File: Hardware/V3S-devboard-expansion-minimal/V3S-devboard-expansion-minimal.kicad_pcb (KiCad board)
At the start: 2 copper layers, 22 x 4 mm, 2 parts, among them CN1 AS0BC21-S30BE-7H, CN2 AS0BC21-S30BE-7H

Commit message: expansion board work
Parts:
- added C1: 100n, Capacitor_SMD:C_0603_1608Metric, F.Cu at (141.1, 61.7)
- added C10: 10u, Capacitor_SMD:C_0603_1608Metric, F.Cu at (145.1, 64.2)
- added C2: 100n, Capacitor_SMD:C_0603_1608Metric, F.Cu at (141.1, 64.2)
- added C3: 10u, Capacitor_SMD:C_0603_1608Metric, F.Cu at (141.1, 66.8)
- added C4: 1u, Capacitor_SMD:C_0603_1608Metric, F.Cu at (141.1, 69.3)
- added C5: 10u, Capacitor_SMD:C_0603_1608Metric, F.Cu at (141.1, 71.8)
- added C6: 1u, Capacitor_SMD:C_0603_1608Metric, F.Cu at (141.1, 74.3)
- added C7: 10u, Capacitor_SMD:C_0603_1608Metric, F.Cu at (141.1, 76.8)
- added C8: 10u, Capacitor_SMD:C_0603_1608Metric, F.Cu at (141.1, 79.3)
- added C9: 10u, Capacitor_SMD:C_0603_1608Metric, F.Cu at (145.1, 61.7)
- added FPC1: AFC07-S50ECA-00, v3s-devboard-expansion-minimal:FPC-SMD_AFC07-S50ECA-00, F.Cu at (95.5, 42.9)
- added J1: Conn_01x05_Pin, Connector_PinHeader_2.54mm:PinHeader_1x05_P2.54mm_Vertical, F.Cu at (42.3, 60.3)
- added J10: USB_C_Receptacle_USB2.0, Connector_USB:USB_C_Receptacle_HCTL_HC-TYPE-C-16P-01A, F.Cu at (73.6, 117.2)
- added J11: Conn_01x02_Pin, Connector_PinHeader_2.54mm:PinHeader_1x02_P2.54mm_Vertical, F.Cu at (45.6, 47.2)
- added J12: Conn_01x02_Pin, Connector_PinHeader_2.54mm:PinHeader_1x02_P2.54mm_Vertical, F.Cu at (50.3, 47.2)
- added J13: Conn_01x03_Pin, Connector_PinSocket_2.54mm:PinSocket_1x03_P2.54mm_Vertical, F.Cu at (31.2, 58.8)
- added J2: Conn_01x05_Pin, Connector_PinHeader_2.54mm:PinHeader_1x05_P2.54mm_Vertical, F.Cu at (47.0, 60.3)
- added J3: Conn_01x05_Pin, Connector_PinHeader_2.54mm:PinHeader_1x05_P2.54mm_Vertical, F.Cu at (51.6, 60.3)
- added J4: Conn_01x02_Pin, Connector_PinHeader_2.54mm:PinHeader_1x02_P2.54mm_Vertical, F.Cu at (36.3, 47.2)
- added J5: Conn_02x05_Odd_Even, Connector_PinHeader_2.54mm:PinHeader_2x05_P2.54mm_Vertical, F.Cu at (56.4, 40.5)
- added J6: Conn_01x02_Pin, Connector_PinHeader_2.54mm:PinHeader_1x02_P2.54mm_Vertical, F.Cu at (41.0, 47.2)
- added J7: Conn_02x12_Odd_Even, Connector_PinSocket_2.54mm:PinSocket_2x12_P2.54mm_Vertical, F.Cu at (36.0, 90.2)
- added J8: RJ45_Hanrun_HR911105A_Horizontal, Connector_RJ:RJ45_Hanrun_HR911105A_Horizontal, F.Cu at (108.8, 103.4)
- added J9: Conn_02x03_Odd_Even, Connector_PinSocket_2.54mm:PinSocket_2x03_P2.54mm_Vertical, F.Cu at (31.7, 41.6)
- added L1: 2.2u, Inductor_SMD:L_1008_2520Metric, F.Cu at (153.6, 62.4)
- added R1: 100, Resistor_SMD:R_0603_1608Metric, F.Cu at (145.1, 66.8)
- added R10: 51, Resistor_SMD:R_0603_1608Metric, F.Cu at (149.1, 66.8)
- added R11: 51, Resistor_SMD:R_0603_1608Metric, F.Cu at (149.1, 69.3)
- added R12: 5.1K, Resistor_SMD:R_0603_1608Metric, F.Cu at (149.1, 71.8)
- added R13: 4.7K, Resistor_SMD:R_0603_1608Metric, F.Cu at (149.1, 74.3)
- added R14: 5.1K, Resistor_SMD:R_0603_1608Metric, F.Cu at (149.1, 76.8)
- added R2: 100, Resistor_SMD:R_0603_1608Metric, F.Cu at (145.1, 69.3)
- added R3: 100, Resistor_SMD:R_0603_1608Metric, F.Cu at (145.1, 71.8)
- added R4: 100, Resistor_SMD:R_0603_1608Metric, F.Cu at (145.1, 74.3)
- added R5: 680, Resistor_SMD:R_0603_1608Metric, F.Cu at (145.1, 76.8)
- added R6: 10k, Resistor_SMD:R_0402_1005Metric, F.Cu at (152.6, 65.2)
- added R7: 680, Resistor_SMD:R_0603_1608Metric, F.Cu at (145.1, 79.3)
- added R8: 51, Resistor_SMD:R_0603_1608Metric, F.Cu at (149.1, 61.7)
- added R9: 51, Resistor_SMD:R_0603_1608Metric, F.Cu at (149.1, 64.2)
- added U1: CP2102N-Axx-xQFN28, Package_DFN_QFN:QFN-28-1EP_5x5mm_P0.5mm_EP3.1x3.1mm, F.Cu at (57.6, 99.0)
- added U2: XDFC-0522-50P, v3s-devboard-expansion-minimal:FPC-SMD_50P-P0.50_LX_XDFC-0522-50P, F.Cu at (95.5, 50.8)
- added U3: AMS1117-3.3, Package_TO_SOT_SMD:SOT-223-3_TabPin2, F.Cu at (78.4, 97.9)
- added U4: AMS1117-2.85, Package_TO_SOT_SMD:SOT-223-3_TabPin2, F.Cu at (70.1, 97.9)
- moved CN2 37.3 mm to (153.9, 112.7)
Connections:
- CN1 pad 76: unconnected-(CN1-Pad76) -> GND
- CN1 pad 77: unconnected-(CN1-Pad77) -> GND

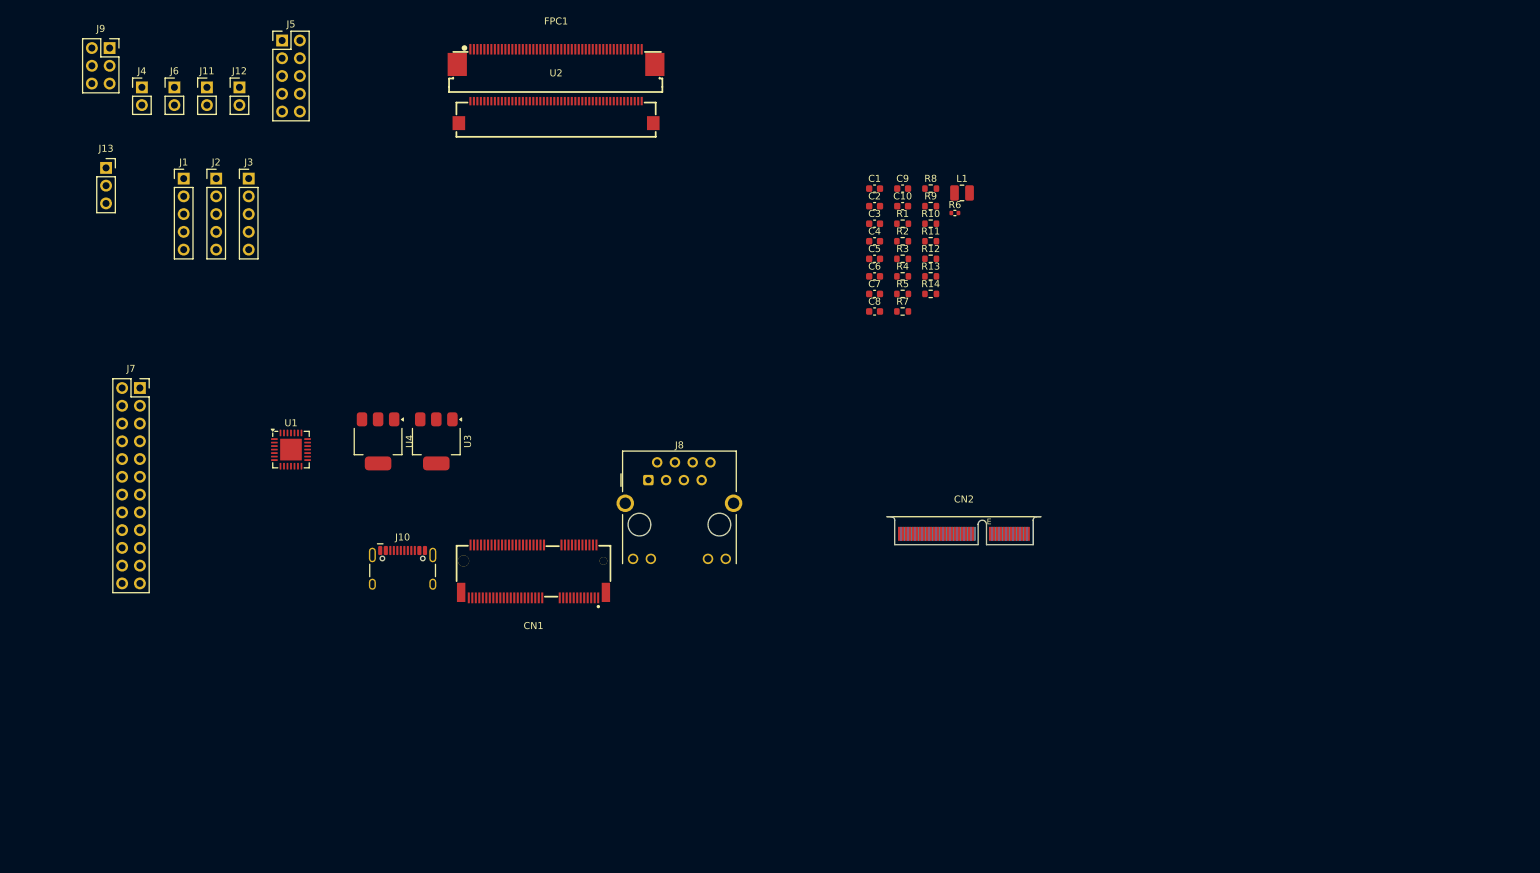
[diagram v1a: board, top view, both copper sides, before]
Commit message: expansion layout and schematic
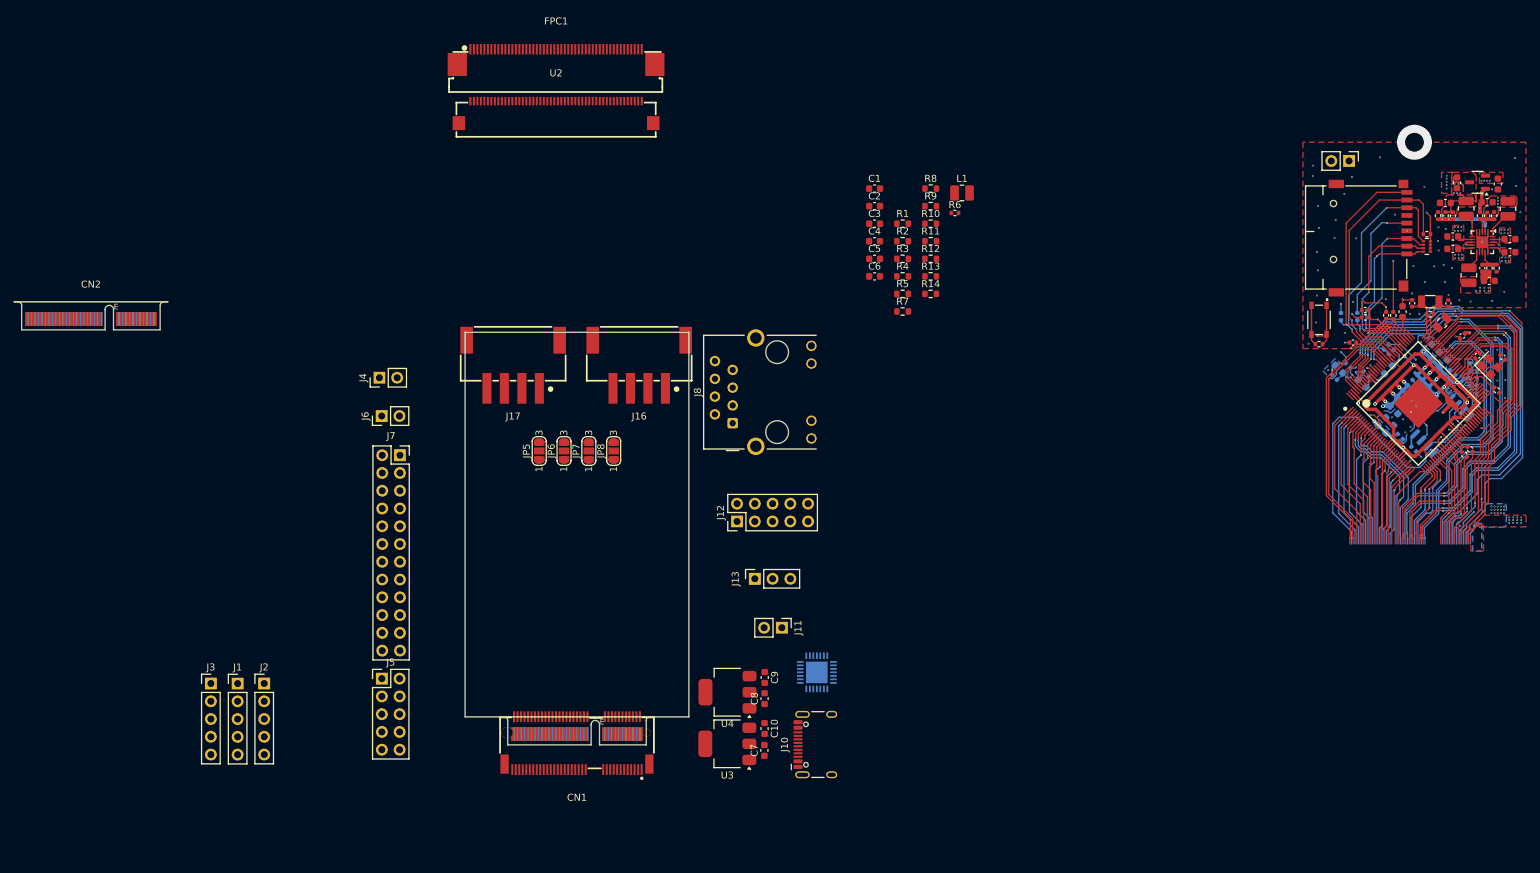
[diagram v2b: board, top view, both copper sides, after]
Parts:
- removed J9: Conn_02x03_Odd_Even, Connector_PinSocket_2.54mm:PinSocket_2x03_P2.54mm_Vertical
- added C101: 1u, Capacitor_SMD:C_0603_1608Metric, F.Cu at (231.9, 70.8)
- added C102: 10u, Capacitor_SMD:C_0603_1608Metric, F.Cu at (231.9, 69.0)
- added C103: 10u, Capacitor_SMD:C_0603_1608Metric, F.Cu at (223.8, 70.3)
- added C104: 10u, Capacitor_SMD:C_0603_1608Metric, F.Cu at (223.8, 68.6)
- added C105: 18p, Capacitor_SMD:C_0402_1005Metric, F.Cu at (228.0, 73.1)
- added C106: 1u, Capacitor_SMD:C_0603_1608Metric, F.Cu at (224.4, 60.9)
- added C107: 1u, Capacitor_SMD:C_0603_1608Metric, F.Cu at (230.2, 61.1)
- added C108: 18p, Capacitor_SMD:C_0402_1005Metric, F.Cu at (223.8, 65.6)
- added C109: 10u, Capacitor_SMD:C_0603_1608Metric, F.Cu at (222.7, 63.8)
- added C110: 18p, Capacitor_SMD:C_0402_1005Metric, F.Cu at (228.7, 65.6)
- added C111: 10u, Capacitor_SMD:C_0603_1608Metric, F.Cu at (228.7, 63.7)
- added C201: 100n, Capacitor_SMD:C_0402_1005Metric, B.Cu at (226.7, 91.1)
- added C202: 100n, Capacitor_SMD:C_0402_1005Metric, B.Cu at (226.7, 89.9)
- added C203: 10u, Capacitor_SMD:C_0603_1608Metric, B.Cu at (221.3, 85.6)
- added C204: 1u, Capacitor_SMD:C_0603_1608Metric, B.Cu at (222.4, 86.7)
- added C205: 100n, Capacitor_SMD:C_0402_1005Metric, B.Cu at (223.8, 88.7)
- added C206: 1u, Capacitor_SMD:C_0603_1608Metric, B.Cu at (220.2, 84.5)
- added C207: 100n, Capacitor_SMD:C_0402_1005Metric, B.Cu at (223.1, 88.0)
- added C208: 10u, Capacitor_SMD:C_0603_1608Metric, B.Cu at (220.7, 91.9)
- added C209: 1u, Capacitor_SMD:C_0603_1608Metric, B.Cu at (219.6, 90.8)
- added C210: 100n, Capacitor_SMD:C_0402_1005Metric, B.Cu at (219.1, 89.5)
- added C211: 100n, Capacitor_SMD:C_0402_1005Metric, B.Cu at (218.4, 88.8)
- added C212: 10u, Capacitor_SMD:C_0603_1608Metric, B.Cu at (213.7, 95.0)
- added C213: 1u, Capacitor_SMD:C_0603_1608Metric, B.Cu at (214.8, 96.1)
- added C214: 100n, Capacitor_SMD:C_0402_1005Metric, B.Cu at (215.6, 97.2)
- added C215: 100n, Capacitor_SMD:C_0402_1005Metric, B.Cu at (216.3, 97.9)
- added C216: 10u, Capacitor_SMD:C_0603_1608Metric, B.Cu at (216.5, 92.3)
- added C217: 1u, Capacitor_SMD:C_0603_1608Metric, B.Cu at (215.4, 93.4)
- added C218: 100n, Capacitor_SMD:C_0402_1005Metric, B.Cu at (217.7, 90.2)
- added C219: 100n, Capacitor_SMD:C_0402_1005Metric, B.Cu at (217.0, 91.0)
- added C220: 100n, Capacitor_SMD:C_0402_1005Metric, F.Cu at (209.5, 83.8)
- added C221: 100n, Capacitor_SMD:C_0402_1005Metric, F.Cu at (225.2, 82.8)
- added C222: 100n, Capacitor_SMD:C_0402_1005Metric, F.Cu at (214.2, 79.8)
- added C223: 100n, Capacitor_SMD:C_0402_1005Metric, B.Cu at (226.7, 86.7)
- added C224: 100n, Capacitor_SMD:C_0402_1005Metric, B.Cu at (208.8, 87.0)
- added C225: 1u, Capacitor_SMD:C_0603_1608Metric, B.Cu at (214.6, 87.6)
- added C226: 4.7u, Capacitor_SMD:C_0603_1608Metric, B.Cu at (210.8, 89.6)
- added C227: 10u, Capacitor_SMD:C_0603_1608Metric, B.Cu at (207.5, 87.5)
- added C228: 100n, Capacitor_SMD:C_0402_1005Metric, B.Cu at (206.9, 88.7)
- added C229: 4.7u, Capacitor_SMD:C_0603_1608Metric, F.Cu at (216.6, 79.3)
- added C230: 18p, Capacitor_SMD:C_0402_1005Metric, F.Cu at (218.0, 78.1)
- added C231: 18p, Capacitor_SMD:C_0402_1005Metric, F.Cu at (223.2, 78.2)
- added C232: 18p, Capacitor_SMD:C_0402_1005Metric, F.Cu at (227.3, 85.7)
- added C233: 18p, Capacitor_SMD:C_0402_1005Metric, F.Cu at (230.9, 85.8)
- added C234: 100n, Capacitor_SMD:C_0402_1005Metric, F.Cu at (211.2, 79.1)
- added C235: 100n, Capacitor_SMD:C_0402_1005Metric, B.Cu at (215.0, 85.1)
- added C236: 100n, Capacitor_SMD:C_0402_1005Metric, B.Cu at (218.2, 99.0)
- added Ce101: 10u, Capacitor_SMD:C_0603_1608Metric, F.Cu at (229.0, 74.9)
- added J101: Conn_01x02, Connector_PinHeader_2.54mm:PinHeader_1x02_P2.54mm_Vertical, F.Cu at (208.9, 57.8)
- added J16: Conn_01x04_MountingPin, v3s-devboard-expansion-minimal:CONN-SMD_HCZZ0021-4, F.Cu at (107.4, 86.8)
- added J17: Conn_01x04_MountingPin, v3s-devboard-expansion-minimal:CONN-SMD_HCZZ0021-4, F.Cu at (89.4, 86.8)
- added J201: Micro_SD_Card_Det1, v3s-devboard-module:J_sd_micro_socket, F.Cu at (210.2, 67.8)
- added J301: AS0BC21-S30BE-7H, v3s-devboard-module:m2-padKeyE, F.Cu at (98.5, 141.3)
- added JP5: SolderJumper_3_Open, Jumper:SolderJumper-3_P1.3mm_Open_RoundedPad1.0x1.5mm_NumberLabels, F.Cu at (93.1, 99.2)
- added JP6: SolderJumper_3_Open, Jumper:SolderJumper-3_P1.3mm_Open_RoundedPad1.0x1.5mm_NumberLabels, F.Cu at (96.7, 99.2)
- added JP7: SolderJumper_3_Open, Jumper:SolderJumper-3_P1.3mm_Open_RoundedPad1.0x1.5mm_NumberLabels, F.Cu at (100.2, 99.2)
- added JP8: SolderJumper_3_Open, Jumper:SolderJumper-3_P1.3mm_Open_RoundedPad1.0x1.5mm_NumberLabels, F.Cu at (103.8, 99.2)
- added L101: 2.2u, Inductor_SMD:L_1008_2520Metric, F.Cu at (226.1, 74.1)
- added L102: 2.2u, Inductor_SMD:L_1008_2520Metric, F.Cu at (225.7, 64.6)
- added L103: 2.2u, Inductor_SMD:L_1008_2520Metric, F.Cu at (231.7, 64.6)
- added R101: 200K, Resistor_SMD:R_0402_1005Metric, F.Cu at (229.0, 73.1)
- added R102: 100K, Resistor_SMD:R_0402_1005Metric, F.Cu at (230.1, 73.1)
- added R103: 680K, Resistor_SMD:R_0402_1005Metric, F.Cu at (222.8, 65.6)
- added R104: 150K, Resistor_SMD:R_0402_1005Metric, F.Cu at (221.7, 65.6)
- added R105: 0, Resistor_SMD:R_0402_1005Metric, F.Cu at (215.3, 79.9)
- added R106: 150K, Resistor_SMD:R_0402_1005Metric, F.Cu at (229.7, 65.6)
- added R107: 150K, Resistor_SMD:R_0402_1005Metric, F.Cu at (227.7, 65.6)
- added R201: 2K, Resistor_SMD:R_0402_1005Metric, B.Cu at (226.7, 88.8)
- added R202: 2K, Resistor_SMD:R_0402_1005Metric, B.Cu at (226.7, 87.8)
- added R203: 200K, Resistor_SMD:R_0402_1005Metric, B.Cu at (211.4, 88.2)
- added R204: 10M, Resistor_SMD:R_0402_1005Metric, F.Cu at (220.6, 79.7)
- added R205: 240, Resistor_SMD:R_0402_1005Metric, F.Cu at (230.1, 90.6)
- added R206: 47K, Resistor_SMD:R_0402_1005Metric, F.Cu at (211.3, 80.2)
- added R207: 6K, Resistor_SMD:R_0805_2012Metric, F.Cu at (222.3, 80.9)
- added R208: 100K, Resistor_SMD:R_0402_1005Metric, B.Cu at (214.3, 84.4)
- added R209: 10K, Resistor_SMD:R_0402_1005Metric, B.Cu at (219.0, 93.9)
- added R210: 0, Resistor_SMD:R_0402_1005Metric, F.Cu at (204.7, 84.0)
- added R211: 33, Resistor_SMD:R_0402_1005Metric, B.Cu at (210.1, 80.0)
- added R212: 33, Resistor_SMD:R_0402_1005Metric, F.Cu at (226.2, 99.0)
- added R213: 33, Resistor_SMD:R_0402_1005Metric, F.Cu at (225.4, 99.8)
- added R214: 47K, Resistor_SMD:R_0402_1005Metric, B.Cu at (207.8, 80.0)
- added R215: 10k, Resistor_SMD:R_0402_1005Metric, F.Cu at (220.1, 68.2)
- added RN201: R_Pack04, Resistor_SMD:R_Array_Concave_4x0402, F.Cu at (220.1, 70.0)
- added SW201: SW_MEC_5E, v3s-devboard-module:SW_SKRPACE010, F.Cu at (204.7, 80.5)
- added U101: EA3036C, Package_DFN_QFN:WQFN-20-1EP_3x3mm_P0.4mm_EP1.7x1.7mm, F.Cu at (228.0, 69.4)
- added U102: XC6206PxxxMR, Package_TO_SOT_SMD:SOT-23-3, F.Cu at (227.3, 60.8)
- added U201: V3S, v3s-devboard-module:LQFP-128_L14.0-W14.0-P0.40-LS16.0-BL-EP5.0, F.Cu at (218.8, 92.5)
- added U202: W25Q128JVS, Package_SO:SOIC-8_5.23x5.23mm_P1.27mm, B.Cu at (222.3, 95.6)
- added Y201: Crystal_Small, Crystal:Crystal_SMD_3215-2Pin_3.2x1.5mm, F.Cu at (220.6, 77.9)
- added Y202: Crystal_GND24_Small, Crystal:Crystal_SMD_2520-4Pin_2.5x2.0mm, F.Cu at (229.1, 87.2)
- J12: value Conn_01x02_Pin -> Conn_02x05_Odd_Even; footprint Connector_PinHeader_2.54mm:PinHeader_1x02_P2.54mm_Vertical -> Connector_PinHeader_2.54mm:PinHeader_2x05_P2.54mm_Vertical
- U1: moved to B.Cu
- moved CN2 128.6 mm to (29.0, 81.9)
- moved J11 112.8 mm to (127.8, 124.5), turned to -90 degrees
- moved J13 109.8 mm to (124.0, 117.5), turned to 90 degrees
- moved J12 94.4 mm to (121.4, 109.3), turned to 90 degrees
- moved J5 92.4 mm to (70.6, 131.8)
- moved U1 81.7 mm to (132.8, 130.9), turned to 180 degrees
- moved C10 77.3 mm to (125.4, 138.9), turned to -90 degrees
- moved C9 72.6 mm to (125.4, 131.6), turned to -90 degrees
- moved J1 72.6 mm to (50.0, 132.5)
- moved J2 72.5 mm to (53.8, 132.5)
- moved J3 72.4 mm to (46.2, 132.5)
- moved C7 67.1 mm to (125.3, 142.1), turned to 90 degrees
- moved J10 64.9 mm to (133.9, 141.2), turned to 90 degrees
- moved U4 61.5 mm to (120.1, 133.8), turned to 180 degrees
- moved U3 60.0 mm to (120.0, 141.1), turned to 180 degrees
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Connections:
- J12 pad 2: Net-(J12-Pin_2) -> /UART0.RX
- U1 pad 25: Net-(J12-Pin_1) -> Net-(J12-Pin_3)
- U1 pad 26: Net-(J12-Pin_2) -> Net-(J12-Pin_1)
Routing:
- net (no net): track 0.00 -> 1896.8 mm, vias 0 -> 108
- net GND: track 0.00 -> 120.8 mm, vias 0 -> 98
- net 3V3: track 0.00 -> 91.8 mm, vias 0 -> 31
- net /CSI.MCSI_MCLK: track 0.00 -> 21.5 mm, vias 0 -> 2
- net /LCD_D23: track 0.00 -> 20.4 mm
- net /LCD_D21: track 0.00 -> 19.5 mm
- net /LCD_D19: track 0.00 -> 18.8 mm
- net /LCD_D15: track 0.00 -> 16.8 mm
- net /LCD_D13: track 0.00 -> 15.9 mm
- net /LCD_D11: track 0.00 -> 15.0 mm
- net /LCD_D7: track 0.00 -> 13.8 mm
- net /LCD_D5: track 0.00 -> 13.2 mm
- net /CSI.CSI_SDA: track 0.00 -> 12.6 mm
- net /LCD_D3: track 0.00 -> 12.4 mm
- net 5V: track 0.00 -> 12.0 mm, vias 0 -> 38
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- added copper zone on F.Cu, net (none)
- added copper zone on F.Cu, net 3V3
- added copper zone on F.Cu, net 5V
- added copper zone on B.Cu, net GND
- added copper zone on F.Cu, net GND
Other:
- board size 22 x 4 mm -> 32 x 55 mm

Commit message: expansion board layout
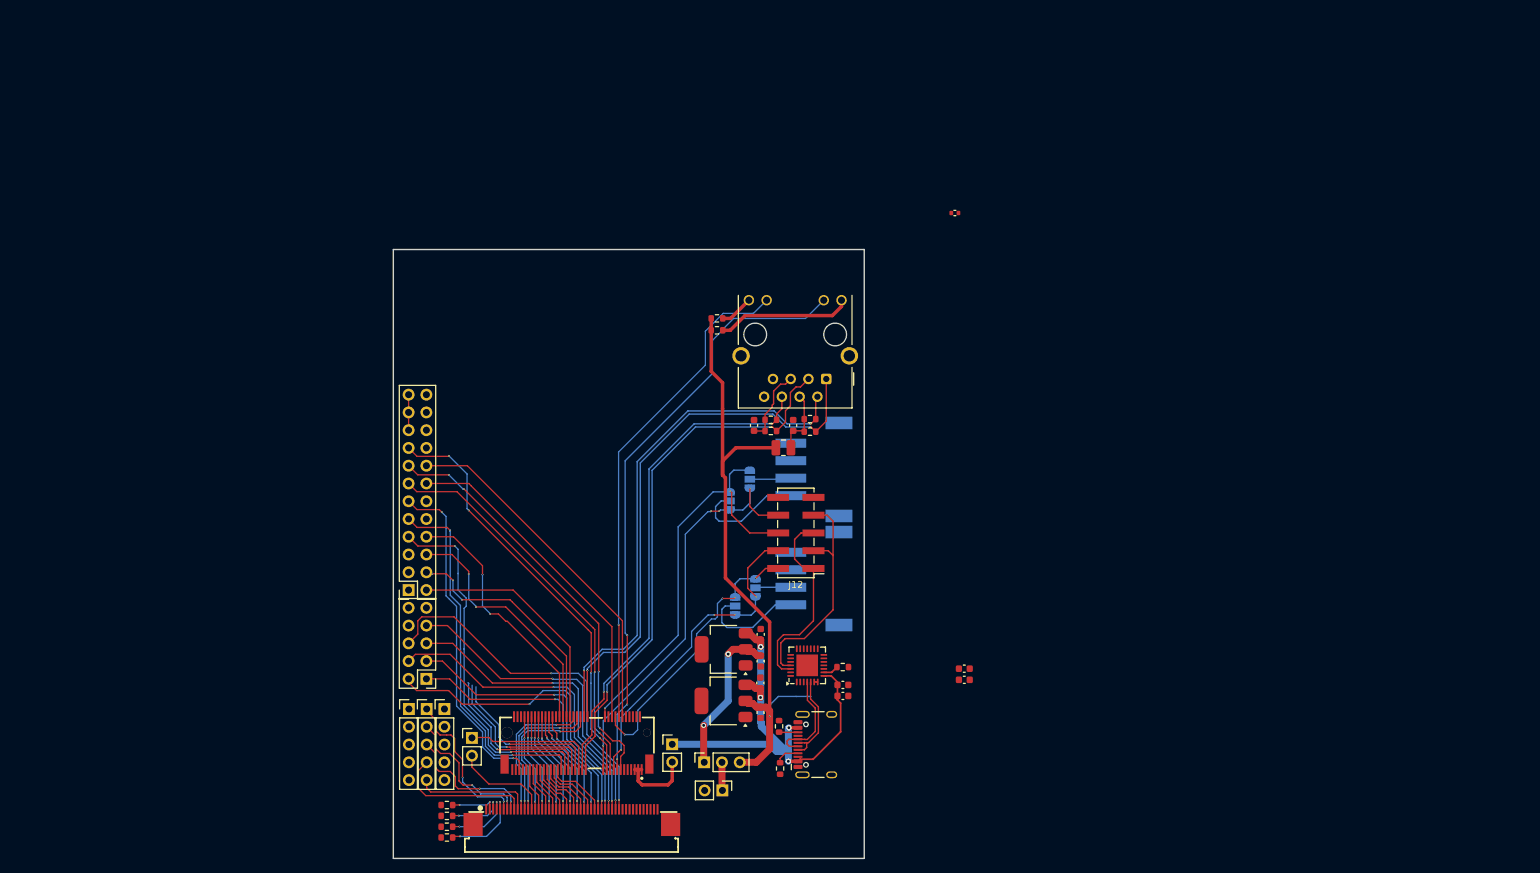
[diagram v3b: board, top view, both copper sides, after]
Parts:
- removed C101, C106, C107, C204, C206, C209, C213, C217, C225: 1u, Capacitor_SMD:C_0603_1608Metric
- removed C102, C103, C104, C109, C111, C203, C208, C212, C216, C227, Ce101: 10u, Capacitor_SMD:C_0603_1608Metric
- removed C105, C108, C110, C230, C231, C232, C233: 18p, Capacitor_SMD:C_0402_1005Metric
- removed C201, C202, C205, C207, C210, C211, C214, C215, C218, C219, C220, C221, C222, C223, C224, C228, C234, C235, C236: 100n, Capacitor_SMD:C_0402_1005Metric
- removed C226, C229: 4.7u, Capacitor_SMD:C_0603_1608Metric
- removed CN2, J301: AS0BC21-S30BE-7H, v3s-devboard-module:m2-padKeyE
- removed J101: Conn_01x02, Connector_PinHeader_2.54mm:PinHeader_1x02_P2.54mm_Vertical
- removed J201: Micro_SD_Card_Det1, v3s-devboard-module:J_sd_micro_socket
- removed L101, L102, L103: 2.2u, Inductor_SMD:L_1008_2520Metric
- removed R101, R203: 200K, Resistor_SMD:R_0402_1005Metric
- removed R102, R208: 100K, Resistor_SMD:R_0402_1005Metric
- removed R103: 680K, Resistor_SMD:R_0402_1005Metric
- removed R104, R106, R107: 150K, Resistor_SMD:R_0402_1005Metric
- removed R105, R210: 0, Resistor_SMD:R_0402_1005Metric
- removed R201, R202: 2K, Resistor_SMD:R_0402_1005Metric
- removed R204: 10M, Resistor_SMD:R_0402_1005Metric
- removed R205: 240, Resistor_SMD:R_0402_1005Metric
- removed R206, R214: 47K, Resistor_SMD:R_0402_1005Metric
- removed R207: 6K, Resistor_SMD:R_0805_2012Metric
- removed R209: 10K, Resistor_SMD:R_0402_1005Metric
- removed R211, R212, R213: 33, Resistor_SMD:R_0402_1005Metric
- removed R215: 10k, Resistor_SMD:R_0402_1005Metric
- removed RN201: R_Pack04, Resistor_SMD:R_Array_Concave_4x0402
- removed SW201: SW_MEC_5E, v3s-devboard-module:SW_SKRPACE010
- removed U101: EA3036C, Package_DFN_QFN:WQFN-20-1EP_3x3mm_P0.4mm_EP1.7x1.7mm
- removed U102: XC6206PxxxMR, Package_TO_SOT_SMD:SOT-23-3
- removed U2: XDFC-0522-50P, v3s-devboard-expansion-minimal:FPC-SMD_50P-P0.50_LX_XDFC-0522-50P
- removed U201: V3S, v3s-devboard-module:LQFP-128_L14.0-W14.0-P0.40-LS16.0-BL-EP5.0
- removed U202: W25Q128JVS, Package_SO:SOIC-8_5.23x5.23mm_P1.27mm
- removed Y201: Crystal_Small, Crystal:Crystal_SMD_3215-2Pin_3.2x1.5mm
- removed Y202: Crystal_GND24_Small, Crystal:Crystal_SMD_2520-4Pin_2.5x2.0mm
- J12: footprint Connector_PinHeader_2.54mm:PinHeader_2x05_P2.54mm_Vertical -> Connector_PinHeader_2.54mm:PinHeader_2x05_P2.54mm_Vertical_SMD
- J16, J17, JP5, JP6, JP7, JP8: moved to B.Cu
- U1: moved to F.Cu
- moved FPC1 108.7 mm to (97.8, 151.6)
- moved R1 105.6 mm to (79.9, 149.9), turned to 180 degrees
- moved R2 104.9 mm to (79.9, 151.4), turned to 180 degrees
- moved R3 104.1 mm to (79.9, 153.0), turned to 180 degrees
- moved R4 103.4 mm to (79.9, 154.5), turned to 180 degrees
- moved J4 76.7 mm to (119.3, 147.8), turned to -90 degrees
- moved R12 76.0 mm to (127.6, 144.7), turned to -90 degrees
- moved C3 67.7 mm to (136.6, 134.3), turned to 180 degrees
- moved R14 65.5 mm to (127.4, 138.6), turned to 90 degrees
- moved C4 63.6 mm to (136.6, 132.7), turned to 180 degrees
- moved C5 61.6 mm to (153.9, 132.0), turned to 180 degrees
- moved C6 57.5 mm to (153.9, 130.4), turned to 180 degrees
- moved R13 57.3 mm to (136.5, 130.2)
- moved J6 47.8 mm to (83.5, 140.3), turned to 0 degrees
- moved J17 45.7 mm to (132.6, 101.9), turned to -90 degrees
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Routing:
- net (no net): track 1896.8 -> 0.00 mm, vias 108 -> 0
- net GND: track 120.8 -> 0.00 mm, vias 98 -> 0
- net /ETH_LED_LINK: track 0.00 -> 85.7 mm, vias 0 -> 3
- net /ETH0.TX_P: track 0.00 -> 78.4 mm, vias 0 -> 2
- net /ETH0.RX_P: track 0.00 -> 77.1 mm, vias 0 -> 2
- net /ETH0.TX_N: track 0.00 -> 74.3 mm, vias 0 -> 2
- net /ETH0.RX_N: track 0.00 -> 71.8 mm, vias 0 -> 2
- net /ETH_LED_SPD: track 0.00 -> 70.9 mm, vias 0 -> 1
- net /VBUS_IN: track 0.00 -> 66.6 mm, vias 0 -> 4
- net /UART2.CTS: track 0.00 -> 60.5 mm, vias 0 -> 4
- net /PB5_PWM1: track 0.00 -> 59.7 mm, vias 0 -> 4
- net /UART2.TX: track 0.00 -> 58.8 mm, vias 0 -> 4
- net /UART2.RX: track 0.00 -> 57.9 mm, vias 0 -> 2
- net /PB6_SCK: track 0.00 -> 56.3 mm, vias 0 -> 2
- net /CSI.CSI_SCK: track 0.00 -> 52.9 mm, vias 0 -> 2
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- removed copper zone on F.Cu, net (none)
- removed copper zone on F.Cu, net 3V3
- removed copper zone on F.Cu, net 5V
- removed copper zone on B.Cu, net GND
- removed copper zone on F.Cu, net GND
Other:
- board size 32 x 55 mm -> 67.3 x 87.1 mm
